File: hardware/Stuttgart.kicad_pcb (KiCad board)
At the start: 2 copper layers, 100 x 50 mm, 45 parts, among them IC1 NCV1117ST33T3G, IC2 UCC12040DVER, IC3 MCP1700T-3302E_TT, IC4 ISO7742DBQR, J1 USB_C_Receptacle_USB2.0_16P, J2 FCR7350, J3 FCR7350, J4 FCR7350, J5 SM03B-SRSS-TB_LF__SN_, U1 RP2354A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

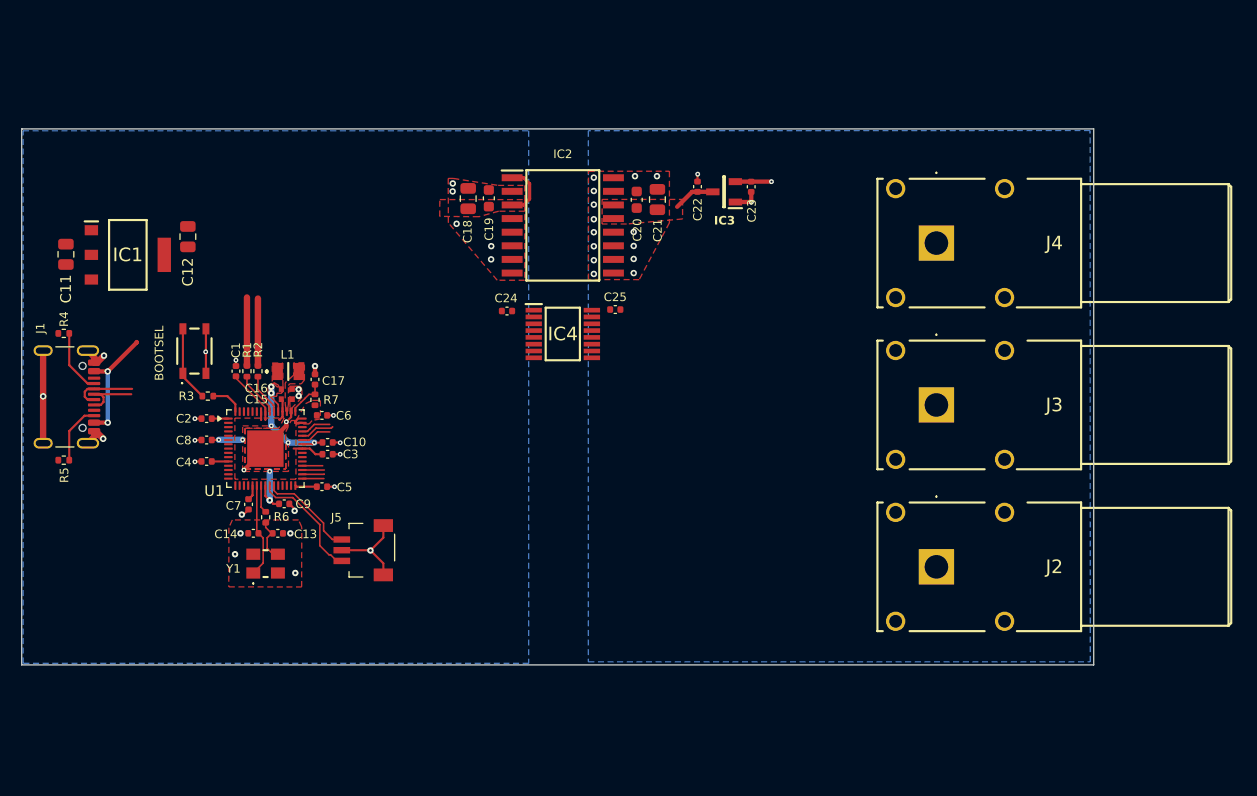
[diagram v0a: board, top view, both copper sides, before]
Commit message: Isolation bridges complete
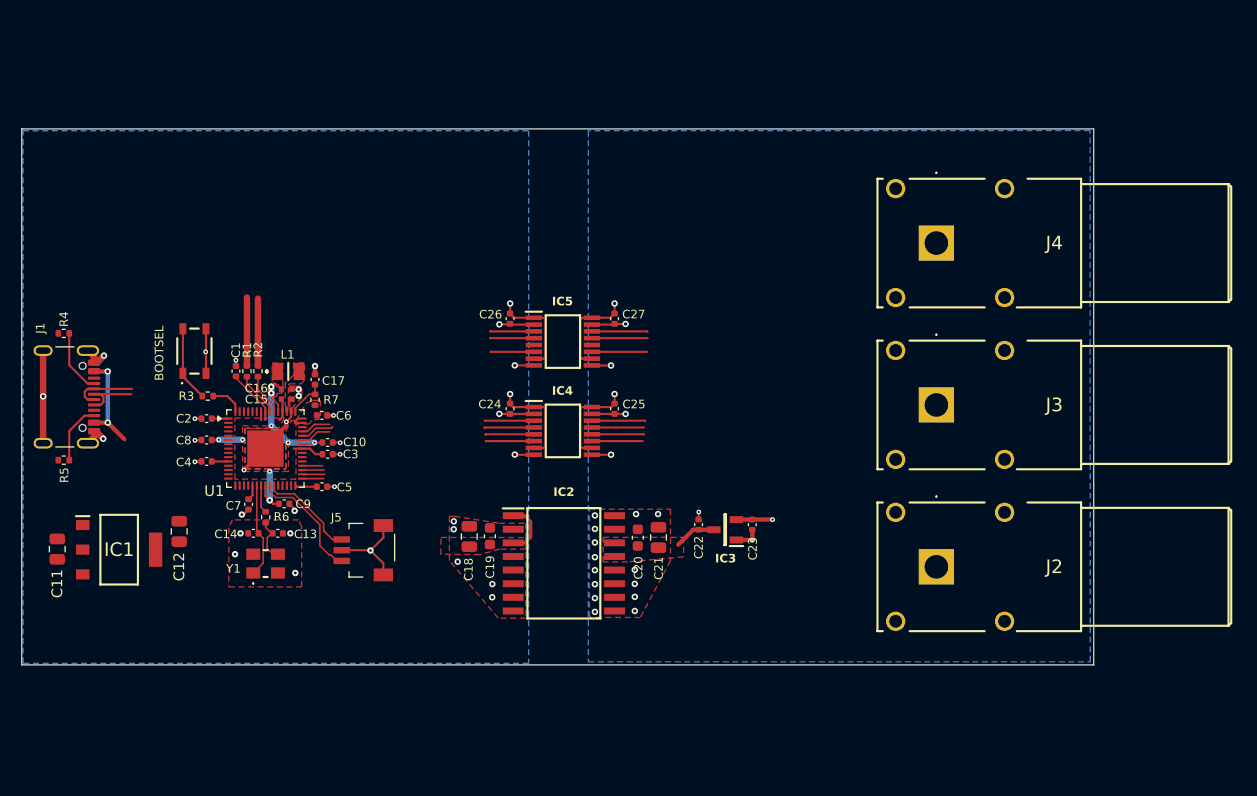
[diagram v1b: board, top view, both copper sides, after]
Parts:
- added C26: 100n, Capacitor_SMD:C_0402_1005Metric, F.Cu at (148.6, 73.2)
- added C27: 100n, Capacitor_SMD:C_0402_1005Metric, F.Cu at (158.3, 73.2)
- added IC5: ISO7741DBQR, Stuttgart:SOP64P600X175-16N, F.Cu at (153.5, 75.3)
- moved C19 31.5 mm to (146.7, 93.5)
- moved C23 31.5 mm to (171.2, 92.4)
- moved IC3 31.5 mm to (168.6, 92.9)
- moved C18 31.5 mm to (144.8, 93.5)
- moved C20 31.5 mm to (160.5, 93.6)
- moved C21 31.5 mm to (162.4, 93.6)
- moved C22 31.5 mm to (166.1, 92.4)
- moved IC2 31.5 mm to (153.6, 96.0)
- moved C11 27.5 mm to (106.3, 94.7)
- moved C12 27.5 mm to (117.7, 93.0)
- moved IC1 27.5 mm to (112.1, 94.8)
- moved C25 9.25 mm to (158.3, 81.6), turned to -90 degrees
- moved C24 9.12 mm to (148.6, 81.6), turned to -90 degrees
- moved IC4 9.04 mm to (153.5, 83.7)
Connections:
- IC4 pad 11: unconnected-(IC4-IND-Pad11) -> SPI0_RX_ISO
- IC4 pad 12: unconnected-(IC4-INC-Pad12) -> CAN_INT_ISO
- IC4 pad 13: unconnected-(IC4-OUTB-Pad13) -> SPI0_TX_ISO
- IC4 pad 14: unconnected-(IC4-OUTA-Pad14) -> SPI0_SCK_ISO
- IC4 pad 3: unconnected-(IC4-INA-Pad3) -> SPI0_SCK
- IC4 pad 4: unconnected-(IC4-INB-Pad4) -> SPI0_TX
- IC4 pad 5: unconnected-(IC4-OUTC-Pad5) -> CAN_INT
- IC4 pad 6: unconnected-(IC4-OUTD-Pad6) -> SPI0_RX
- U1 pad 31: /RP2354A/SPI0_TX -> SPI0_TX
- U1 pad 32: /RP2354A/SPI0_RX -> SPI0_RX
- U1 pad 33: /RP2354A/CAN_STBY -> CAN_INT
- U1 pad 34: /RP2354A/SPI0_SCK -> SPI0_SCK
- U1 pad 40: /RP2354A/SPI1_SCK -> SPI1_SCK
- U1 pad 41: /RP2354A/SPI1_TX -> SPI1_TX
- U1 pad 42: /RP2354A/SPI1_RX -> SPI1_RX
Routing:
- net +3V3: track 19.0 -> 37.2 mm, vias 0 -> 2
- net +3.3VA: track 3.37 -> 21.3 mm, vias 1 -> 3
- net GND: track 41.0 -> 51.1 mm, vias 29 -> 33
- net GND1: track 3.94 -> 13.6 mm, vias 16 -> 20
- net SPI1_TX: track 0.00 -> 7.27 mm
- net SPI1_SCK: track 0.00 -> 6.93 mm
- net SPI1_RX: track 0.00 -> 6.85 mm
- net SPI0_TX: track 0.00 -> 6.61 mm
- net CAN_INT: track 0.00 -> 6.58 mm
- net SPI0_RX: track 0.00 -> 6.55 mm
- net SPI0_SCK: track 0.00 -> 6.47 mm
- net SPI1_SCK_ISO: track 0.00 -> 5.20 mm
- net SPI1_TX_ISO: track 0.00 -> 5.17 mm
- net SPI1_RX_ISO: track 0.00 -> 5.17 mm
- net SPI0_SCK_ISO: track 0.00 -> 4.95 mm
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
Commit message: CAN ADC on the board
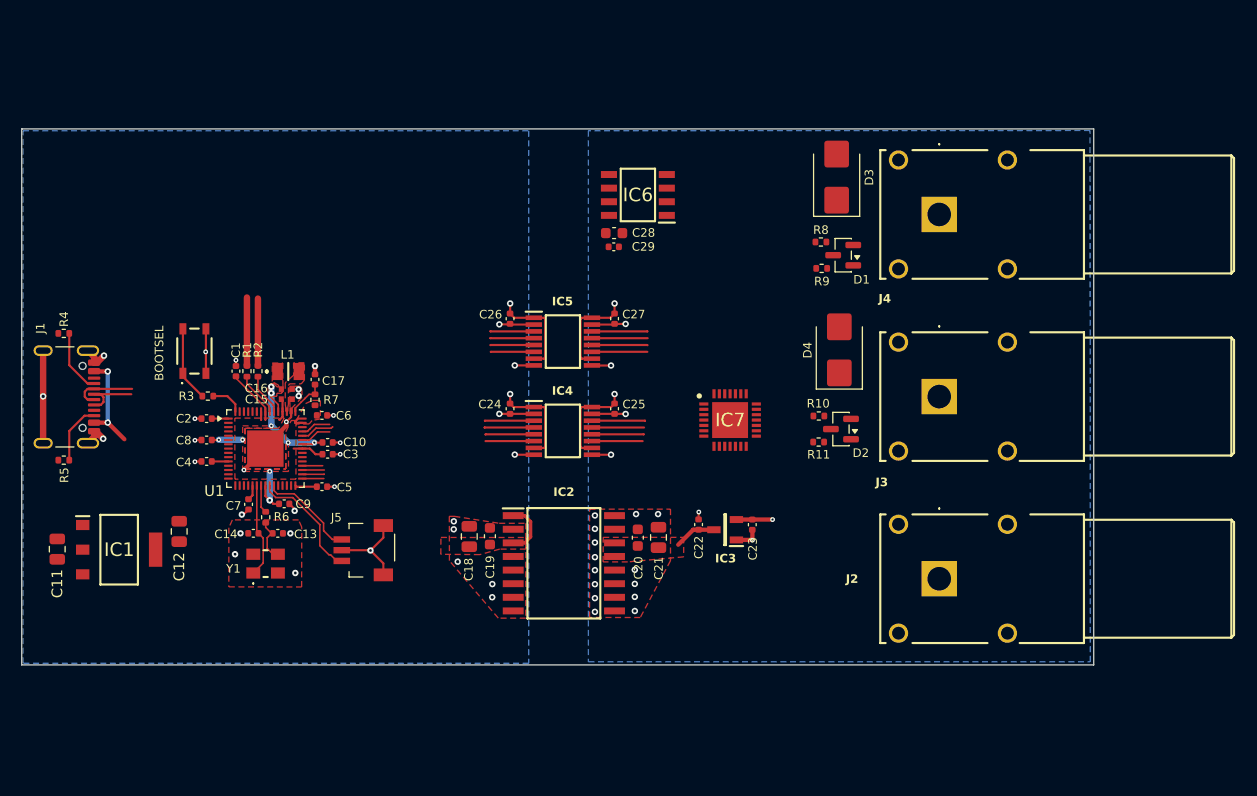
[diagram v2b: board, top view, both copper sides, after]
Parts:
- added C28: 10u, Capacitor_SMD:C_0603_1608Metric, F.Cu at (158.3, 65.2)
- added C29: 100n, Capacitor_SMD:C_0402_1005Metric, F.Cu at (158.2, 66.5)
- added D1: BZX84Cxx, Package_TO_SOT_SMD:SOT-23, F.Cu at (179.6, 67.3)
- added D2: BZX84Cxx, Package_TO_SOT_SMD:SOT-23, F.Cu at (179.4, 83.5)
- added D3: SM6T6V8A, Diode_SMD:D_SMB, F.Cu at (179.0, 60.0)
- added D4: SM6T6V8A, Diode_SMD:D_SMB, F.Cu at (179.3, 76.1)
- added IC6: MCP3202-CI_SN, Stuttgart:SOIC127P600X175-8N, F.Cu at (160.5, 61.7)
- added IC7: MCP251863T-E_9PX, Stuttgart:QFN50P500X500X90-29N-D, F.Cu at (169.1, 82.7)
- added R10: 10k, Resistor_SMD:R_0402_1005Metric, F.Cu at (177.4, 82.3)
- added R11: 47k, Resistor_SMD:R_0402_1005Metric, F.Cu at (177.3, 84.7)
- added R8: 10k, Resistor_SMD:R_0402_1005Metric, F.Cu at (177.6, 66.0)
- added R9: 47k, Resistor_SMD:R_0402_1005Metric, F.Cu at (177.6, 68.5)
- J2: value FCR7350 -> FCR7350B
- J3: value FCR7350 -> FCR7350G
- J4: value FCR7350 -> FCR7350Y
- moved J4 2.68 mm to (188.6, 63.5)
- moved J2 1.14 mm to (188.6, 97.5)
- moved J3 0.82 mm to (188.6, 80.5)
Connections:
- IC5 pad 12: unconnected-(IC5-OUTC-Pad12) -> ADC_CONV_ISO
- IC5 pad 5: unconnected-(IC5-INC-Pad5) -> ADC_CONV
- J2 pad 1: unconnected-(J2-Pad1) -> GND1
- J3 pad 1: unconnected-(J3-Pad1) -> /Vehicle Interface/CAN_L
- J4 pad 1: unconnected-(J4-Pad1) -> /Vehicle Interface/CAN_H
- U1 pad 43: unconnected-(U1-GPIO29/ADC3-Pad43) -> ADC_CONV
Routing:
- net ADC_CONV_ISO: track 0.00 -> 5.18 mm
- net ADC_CONV: track 0.00 -> 4.05 mm

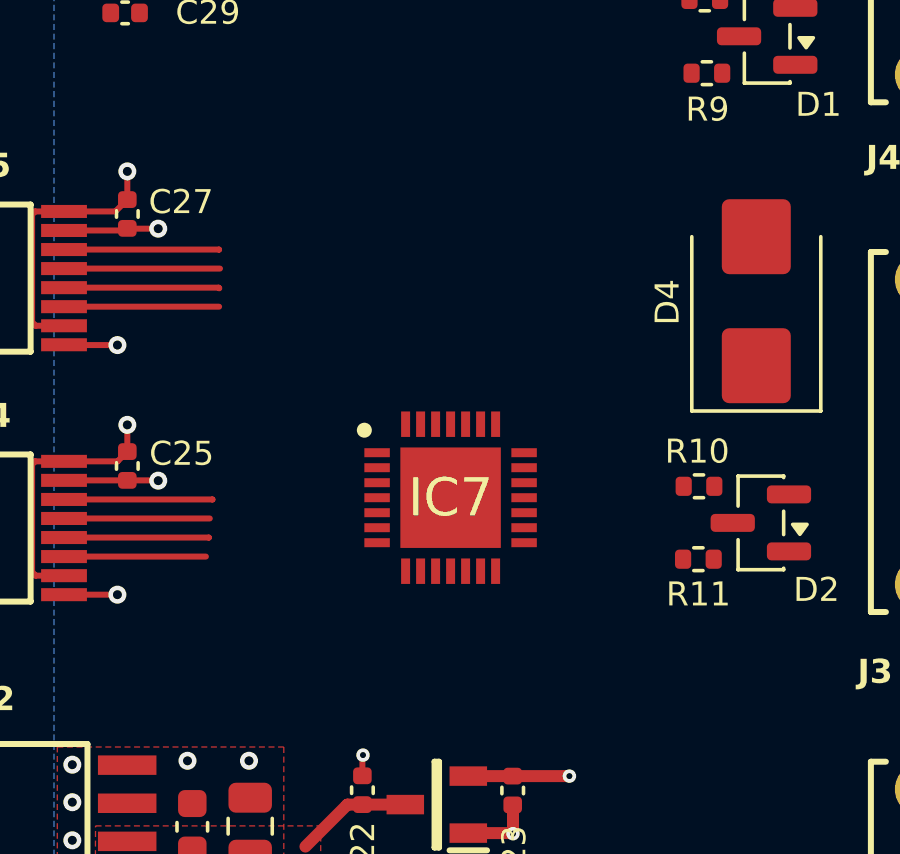
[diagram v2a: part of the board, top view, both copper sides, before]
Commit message: Further CAN IC work before reworking SPI bridges
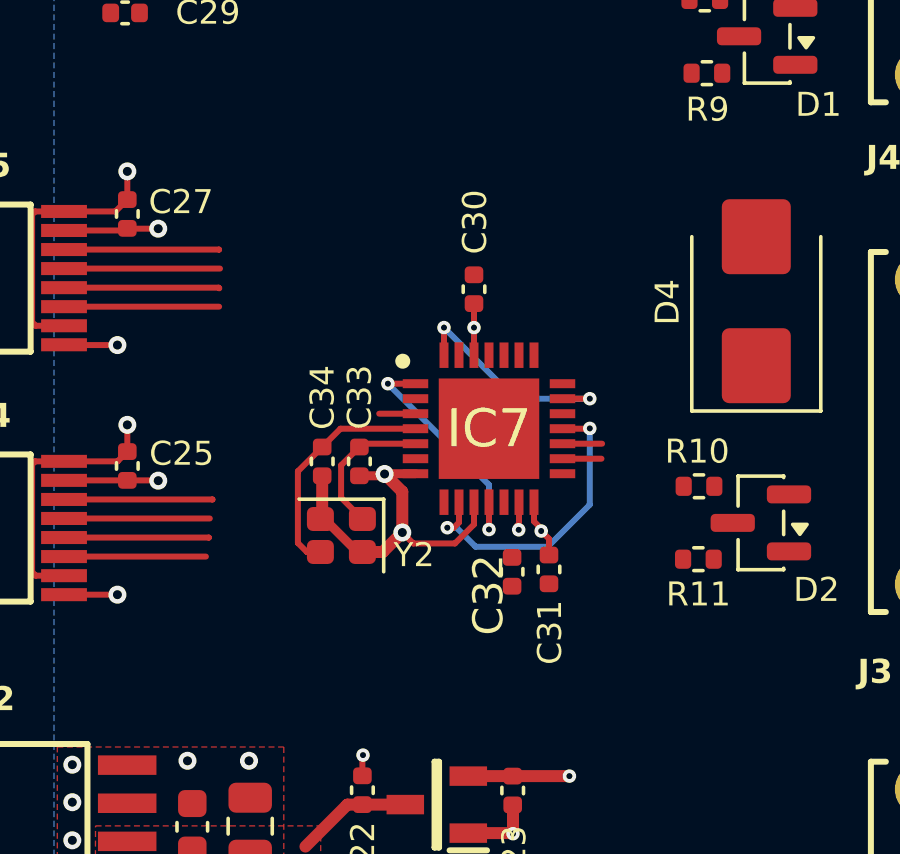
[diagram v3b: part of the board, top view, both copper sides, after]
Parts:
- added C30: 100n, Capacitor_SMD:C_0402_1005Metric, F.Cu at (169.9, 75.7)
- added C31: 100n, Capacitor_SMD:C_0402_1005Metric, F.Cu at (172.4, 85.0)
- added C32: 100n, Capacitor_SMD:C_0402_1005Metric, F.Cu at (171.1, 85.1)
- added C33: 6p, Capacitor_SMD:C_0402_1005Metric, F.Cu at (166.0, 81.5)
- added C34: 6p, Capacitor_SMD:C_0402_1005Metric, F.Cu at (164.8, 81.5)
- added Y2: Crystal_GND24, Crystal:Crystal_SMD_2016-4Pin_2.0x1.6mm, F.Cu at (165.4, 83.9)
- moved IC7 2.63 mm to (170.4, 80.4)
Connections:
- IC7 pad 1: unconnected-(IC7-RXCAN-Pad1) -> /Vehicle Interface/RXCAN
- IC7 pad 10: unconnected-(IC7-GND-Pad10) -> GND1
- IC7 pad 11: unconnected-(IC7-RXD-Pad11) -> /Vehicle Interface/RXCAN
- IC7 pad 13: unconnected-(IC7-VCC-Pad13) -> +5V
- IC7 pad 14: unconnected-(IC7-VIO-Pad14) -> +3.3VA
- IC7 pad 16: unconnected-(IC7-CANL-Pad16) -> /Vehicle Interface/CAN_L
- IC7 pad 17: unconnected-(IC7-CANH-Pad17) -> /Vehicle Interface/CAN_H
- IC7 pad 18: unconnected-(IC7-STBY-Pad18) -> /Vehicle Interface/STBY
- IC7 pad 20: unconnected-(IC7-TXD-Pad20) -> /Vehicle Interface/TXCAN
- IC7 pad 22: unconnected-(IC7-SCK-Pad22) -> SPI0_SCK_ISO
- IC7 pad 23: unconnected-(IC7-SDI-Pad23) -> SPI0_TX_ISO
- IC7 pad 24: unconnected-(IC7-SDO-Pad24) -> SPI0_RX_ISO
- IC7 pad 26: unconnected-(IC7-VDD-Pad26) -> +3.3VA
- IC7 pad 28: unconnected-(IC7-TXCAN-Pad28) -> /Vehicle Interface/TXCAN
- IC7 pad 3: unconnected-(IC7-NINT-Pad3) -> CAN_INT_ISO
- IC7 pad 4: unconnected-(IC7-OSC2-Pad4) -> /Vehicle Interface/OSC2
- IC7 pad 5: unconnected-(IC7-OSC1-Pad5) -> /Vehicle Interface/OSC1
- IC7 pad 7: unconnected-(IC7-VSS-Pad7) -> GND1
- IC7 pad 9: unconnected-(IC7-NINT0/GPIO0/XSTBY-Pad9) -> /Vehicle Interface/STBY
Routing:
- net GND1: track 13.6 -> 25.8 mm, vias 20 -> 22
- net /Vehicle Interface/STBY: track 0.00 -> 10.1 mm, vias 0 -> 2
- net /Vehicle Interface/RXCAN: track 0.00 -> 7.96 mm, vias 0 -> 2
- net /Vehicle Interface/OSC2: track 0.00 -> 7.77 mm
- net /Vehicle Interface/TXCAN: track 0.00 -> 7.67 mm, vias 0 -> 2
- net /Vehicle Interface/OSC1: track 0.00 -> 4.86 mm
- net +3.3VA: track 21.3 -> 24.9 mm, vias 3 -> 5
- net /Vehicle Interface/CAN_H: track 0.00 -> 1.32 mm
- net /Vehicle Interface/CAN_L: track 0.00 -> 1.30 mm
- net CAN_INT_ISO: track 4.83 -> 6.04 mm
- net +5V: track 3.91 -> 4.73 mm, vias 0 -> 1

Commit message: Further iso bridge development
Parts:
- IC4: value ISO7742DBQR -> ISO7763DBQR
- moved IC4 1.48 mm to (153.3, 85.1)
- moved C5 0.78 mm to (130.8, 89.6)
- moved C30 0.70 mm to (169.3, 76.1), turned to 180 degrees
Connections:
- net ADC_CONV renamed SPI1_CS
- net ADC_CONV_ISO renamed SPI1_CS_ISO
- IC4 pad 10: +3.3VA -> CAN_INT1_ISO
- IC4 pad 11: SPI0_RX_ISO -> CAN_INT_ISO
- IC4 pad 12: CAN_INT_ISO -> SPI0_RX_ISO
- IC4 pad 13: SPI0_TX_ISO -> SPI0_CS_ISO
- IC4 pad 14: SPI0_SCK_ISO -> SPI0_TX_ISO
- IC4 pad 15: GND1 -> SPI0_SCK_ISO
- IC4 pad 2: GND -> SPI0_SCK
- IC4 pad 3: SPI0_SCK -> SPI0_TX
- IC4 pad 4: SPI0_TX -> SPI0_CS
- IC4 pad 5: CAN_INT -> SPI0_RX
- IC4 pad 6: SPI0_RX -> CAN_INT
- IC4 pad 7: +3V3 -> CAN_INT1
- IC7 pad 25: unconnected-(IC7-NCS-Pad25) -> SPI0_CS_ISO
- IC7 pad 8: unconnected-(IC7-NINT1/GPIO1-Pad8) -> CAN_INT1_ISO
- U1 pad 33: CAN_INT -> SPI0_CS
- U1 pad 35: unconnected-(U1-GPIO23-Pad35) -> CAN_INT
- U1 pad 36: unconnected-(U1-GPIO24-Pad36) -> CAN_INT1
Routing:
- net CAN_INT1: track 0.00 -> 15.2 mm, vias 0 -> 2
- net SPI0_CS: track 0.00 -> 12.5 mm
- net SPI0_CS_ISO: track 0.00 -> 8.78 mm
- net CAN_INT: track 6.58 -> 14.6 mm, vias 0 -> 2
- net +3V3: track 37.2 -> 29.8 mm
- net CAN_INT1_ISO: track 0.00 -> 7.35 mm, vias 0 -> 2
- net SPI0_SCK_ISO: track 4.95 -> 11.8 mm
- net SPI0_TX: track 6.61 -> 13.2 mm, vias 0 -> 2
- net SPI0_SCK: track 6.47 -> 12.9 mm
- net SPI0_RX: track 6.55 -> 12.4 mm
- net +3.3VA: track 24.9 -> 19.1 mm
- net SPI0_TX_ISO: track 4.86 -> 10.6 mm
- net GND: track 51.1 -> 47.1 mm, vias 33 -> 32
- net SPI0_RX_ISO: track 4.73 -> 8.71 mm, vias 0 -> 2
- net SPI1_CS: track 4.05 -> 7.39 mm
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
